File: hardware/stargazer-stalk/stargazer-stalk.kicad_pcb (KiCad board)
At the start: 2 copper layers, 8 parts, among them U10 pmod-interface-type-2a, U12 pmod-interface-type-2a, U14 pmod-interface-type-2a, U18 pmod-interface-type-2a, U2 pmod-interface-type-2a, U4 pmod-interface-type-2a, U6 pmod-interface-type-2a, U8 pmod-interface-type-2a

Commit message: Working before reworking to a 4 card system
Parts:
- added C1: 0.1uF, Capacitor_SMD:C_0805_2012Metric, F.Cu at (204.5, 20.3)
- added C10: 0.1uF, Capacitor_SMD:C_0805_2012Metric, F.Cu at (115.7, 131.3)
- added C2: 0.1uF, Capacitor_SMD:C_0805_2012Metric, F.Cu at (125.7, 60.3)
- added C3: 0.1uF, Capacitor_SMD:C_0805_2012Metric, F.Cu at (154.1, 126.1)
- added C4: 0.1uF, Capacitor_SMD:C_0805_2012Metric, F.Cu at (87.6, 60.9)
- added C5: 0.1uF, Capacitor_SMD:C_0805_2012Metric, F.Cu at (189.6, 100.5)
- added C6: 0.1uF, Capacitor_SMD:C_0805_2012Metric, F.Cu at (49.9, 90.6)
- added C7: 0.1uF, Capacitor_SMD:C_0805_2012Metric, F.Cu at (159.7, 63.9)
- added C8: 0.1uF, Capacitor_SMD:C_0805_2012Metric, F.Cu at (87.0, 131.9)
- added J1: swd-basic, Connector_PinHeader_2.54mm:PinHeader_1x04_P2.54mm_Vertical, F.Cu at (125.0, 126.7)
- added J2: swd-basic, Connector_PinHeader_2.54mm:PinHeader_1x04_P2.54mm_Vertical, F.Cu at (116.8, 51.0)
- added J3: swd-basic, Connector_PinHeader_2.54mm:PinHeader_1x04_P2.54mm_Vertical, F.Cu at (165.5, 126.2)
- added J4: swd-basic, Connector_PinHeader_2.54mm:PinHeader_1x04_P2.54mm_Vertical, F.Cu at (78.7, 51.5)
- added J5: swd-basic, Connector_PinHeader_2.54mm:PinHeader_1x04_P2.54mm_Vertical, F.Cu at (189.7, 89.1)
- added J6: swd-basic, Connector_PinHeader_2.54mm:PinHeader_1x04_P2.54mm_Vertical, F.Cu at (49.8, 102.0)
- added J7: swd-basic, Connector_PinHeader_2.54mm:PinHeader_1x04_P2.54mm_Vertical, F.Cu at (155.4, 51.5)
- added J8: swd-basic, Connector_PinHeader_2.54mm:PinHeader_1x04_P2.54mm_Vertical, F.Cu at (74.7, 132.2)
- added JP1: SolderJumper_3_Bridged12, Jumper:SolderJumper-3_P1.3mm_Bridged12_RoundedPad1.0x1.5mm, F.Cu at (182.7, 32.3)
- added JP10: SolderJumper_2_Bridged, Jumper:SolderJumper-2_P1.3mm_Bridged_RoundedPad1.0x1.5mm, F.Cu at (197.7, 32.4)
- added JP11: SolderJumper_2_Bridged, Jumper:SolderJumper-2_P1.3mm_Bridged_RoundedPad1.0x1.5mm, F.Cu at (203.4, 26.5)
- added JP2: SolderJumper_3_Bridged12, Jumper:SolderJumper-3_P1.3mm_Bridged12_RoundedPad1.0x1.5mm, F.Cu at (195.0, 20.6)
- added JP3: SolderJumper_3_Bridged12, Jumper:SolderJumper-3_P1.3mm_Bridged12_RoundedPad1.0x1.5mm, F.Cu at (188.3, 32.3)
- added JP4: SolderJumper_2_Bridged, Jumper:SolderJumper-2_P1.3mm_Bridged_RoundedPad1.0x1.5mm, F.Cu at (208.8, 24.2)
- added JP5: SolderJumper_2_Bridged, Jumper:SolderJumper-2_P1.3mm_Bridged_RoundedPad1.0x1.5mm, F.Cu at (202.1, 33.6)
- added JP6: SolderJumper_2_Bridged, Jumper:SolderJumper-2_P1.3mm_Bridged_RoundedPad1.0x1.5mm, F.Cu at (207.8, 27.7)
- added JP7: SolderJumper_2_Bridged, Jumper:SolderJumper-2_P1.3mm_Bridged_RoundedPad1.0x1.5mm, F.Cu at (207.6, 31.3)
- added JP8: SolderJumper_2_Bridged, Jumper:SolderJumper-2_P1.3mm_Bridged_RoundedPad1.0x1.5mm, F.Cu at (208.8, 20.6)
- added JP9: SolderJumper_2_Bridged, Jumper:SolderJumper-2_P1.3mm_Bridged_RoundedPad1.0x1.5mm, F.Cu at (203.2, 30.1)
- added R1: 100k, Resistor_SMD:R_0805_2012Metric, F.Cu at (121.1, 63.3)
- added R10: 10k, Resistor_SMD:R_0805_2012Metric, F.Cu at (204.5, 23.3)
- added R11: 10k, Resistor_SMD:R_0805_2012Metric, F.Cu at (193.4, 34.9)
- added R12: 10k, Resistor_SMD:R_0805_2012Metric, F.Cu at (198.8, 29.2)
- added R13: 100k, Resistor_SMD:R_0805_2012Metric, F.Cu at (83.0, 63.9)
- added R14: 100k, Resistor_SMD:R_0805_2012Metric, F.Cu at (198.7, 98.4)
- added R15: 100k, Resistor_SMD:R_0805_2012Metric, F.Cu at (194.0, 101.4)
- added R16: 100k, Resistor_SMD:R_0805_2012Metric, F.Cu at (194.2, 98.4)
- added R17: 100k, Resistor_SMD:R_0805_2012Metric, F.Cu at (40.8, 92.7)
- added R18: 100k, Resistor_SMD:R_0805_2012Metric, F.Cu at (45.5, 89.7)
- added R19: 100k, Resistor_SMD:R_0805_2012Metric, F.Cu at (45.2, 92.7)
- added R2: 100k, Resistor_SMD:R_0805_2012Metric, F.Cu at (121.3, 60.3)
- added R20: 100k, Resistor_SMD:R_0805_2012Metric, F.Cu at (164.4, 60.9)
- added R21: 10k, Resistor_SMD:R_0805_2012Metric, F.Cu at (193.4, 32.0)
- added R22: 10k, Resistor_SMD:R_0805_2012Metric, F.Cu at (194.4, 28.8)
- added R23: 10k, Resistor_SMD:R_0805_2012Metric, F.Cu at (200.1, 23.3)
- added R24: 10k, Resistor_SMD:R_0805_2012Metric, F.Cu at (200.1, 20.3)
- added R25: 100k, Resistor_SMD:R_0805_2012Metric, F.Cu at (159.9, 60.9)
- added R26: 100k, Resistor_SMD:R_0805_2012Metric, F.Cu at (155.3, 62.9)
- added R27: 100k, Resistor_SMD:R_0805_2012Metric, F.Cu at (84.1, 127.2)
- added R28: 100k, Resistor_SMD:R_0805_2012Metric, F.Cu at (87.0, 127.5)
- added R29: 100k, Resistor_SMD:R_0805_2012Metric, F.Cu at (85.0, 122.8)
- added R3: 100k, Resistor_SMD:R_0805_2012Metric, F.Cu at (116.7, 62.4)
- added R33: 100k, Resistor_SMD:R_0805_2012Metric, F.Cu at (112.7, 131.0)
- added R34: 100k, Resistor_SMD:R_0805_2012Metric, F.Cu at (115.7, 135.7)
- added R35: 100k, Resistor_SMD:R_0805_2012Metric, F.Cu at (113.6, 126.6)
- added R4: 100k, Resistor_SMD:R_0805_2012Metric, F.Cu at (156.2, 135.2)
- added R5: 100k, Resistor_SMD:R_0805_2012Metric, F.Cu at (153.2, 130.5)
- added R6: 100k, Resistor_SMD:R_0805_2012Metric, F.Cu at (156.2, 130.8)
- added R7: 100k, Resistor_SMD:R_0805_2012Metric, F.Cu at (78.6, 62.9)
- added R8: 100k, Resistor_SMD:R_0805_2012Metric, F.Cu at (83.2, 60.9)
- added R9: 10k, Resistor_SMD:R_0805_2012Metric, F.Cu at (199.1, 26.2)
- added TP1: TestPoint, Connector_PinHeader_2.54mm:PinHeader_1x01_P2.54mm_Vertical, F.Cu at (194.5, 25.0)
- added U1: SN74LVC125AD, Package_SO:SOIC-14_3.9x8.7mm_P1.27mm, F.Cu at (108.0, 80.0)
- added U11: SN74LVC125AD, Package_SO:SOIC-14_3.9x8.7mm_P1.27mm, F.Cu at (146.1, 80.0)
- added U13: SN74LVC125AD, Package_SO:SOIC-14_3.9x8.7mm_P1.27mm, F.Cu at (95.2, 110.5)
- added U16: PCF8574, stargazer-stalk:SOIC127P1032X265-16N, F.Cu at (186.0, 24.7)
- added U17: SN74LVC125AD, Package_SO:SOIC-14_3.9x8.7mm_P1.27mm, F.Cu at (133.3, 110.5)
- added U3: SN74LVC125AD, Package_SO:SOIC-14_3.9x8.7mm_P1.27mm, F.Cu at (171.4, 110.5)
- added U5: SN74LVC125AD, Package_SO:SOIC-14_3.9x8.7mm_P1.27mm, F.Cu at (69.8, 80.0)
- added U7: SN74LVC125AD, Package_SO:SOIC-14_3.9x8.7mm_P1.27mm, F.Cu at (174.0, 82.5)
- added U9: SN74LVC125AD, Package_SO:SOIC-14_3.9x8.7mm_P1.27mm, F.Cu at (67.3, 108.0)
- moved U10 89.3 mm to (69.8, 102.9), turned to 180 degrees
- moved U6 83.9 mm to (74.9, 82.5)
- moved U18 63.5 mm to (128.3, 108.0), turned to 270 degrees
- moved U4 54.3 mm to (166.4, 108.0), turned to 270 degrees
- moved U12 42.2 mm to (151.1, 82.5), turned to 90 degrees
- moved U2 30.7 mm to (113.0, 82.5)
- moved U14 8.52 mm to (90.2, 108.0)
- moved U8 8.52 mm to (171.4, 87.6)
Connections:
- U10 pad 1: /card-6/CSn1 -> /card-6/CSn
- U10 pad 10: /card-6/SWCLK1 -> /card-6/SWCLK
- U10 pad 2: /card-6/COPI1 -> /card-6/COPI
- U10 pad 3: /card-6/CIPO1 -> /card-6/CIPO
- U10 pad 4: /card-6/SCK1 -> /card-6/SCK
- U10 pad 7: /card-6/GO1 -> /card-6/GO
- U10 pad 8: /card-6/RST1 -> /card-6/RST
- U10 pad 9: /card-6/SWDIO1 -> /card-6/SWDIO
- U12 pad 1: /card-7/CSn1 -> /card-7/CSn
- U12 pad 10: /card-7/SWCLK1 -> /card-7/SWCLK
- U12 pad 2: /card-7/COPI1 -> /card-7/COPI
- U12 pad 3: /card-7/CIPO1 -> /card-7/CIPO
- U12 pad 4: /card-7/SCK1 -> /card-7/SCK
- U12 pad 7: /card-7/GO1 -> /card-7/GO
- U12 pad 8: /card-7/RST1 -> /card-7/RST
- U12 pad 9: /card-7/SWDIO1 -> /card-7/SWDIO
- U14 pad 1: /card-8/CSn1 -> /card-8/CSn
- U14 pad 10: /card-8/SWCLK1 -> /card-8/SWCLK
- U14 pad 2: /card-8/COPI1 -> /card-8/COPI
- U14 pad 3: /card-8/CIPO1 -> /card-8/CIPO
- U14 pad 4: /card-8/SCK1 -> /card-8/SCK
- U14 pad 7: /card-8/GO1 -> /card-8/GO
- U14 pad 8: /card-8/RST1 -> /card-8/RST
- U14 pad 9: /card-8/SWDIO1 -> /card-8/SWDIO
- U18 pad 1: /card-1/CSn1 -> /card-1/CSn
- U18 pad 10: /card-1/SWCLK1 -> /card-1/SWCLK
- U18 pad 2: /card-1/COPI1 -> /card-1/COPI
- U18 pad 3: /card-1/CIPO1 -> /card-1/CIPO
- U18 pad 4: /card-1/SCK1 -> /card-1/SCK
- U18 pad 7: /card-1/GO1 -> /card-1/GO
- U18 pad 8: /card-1/RST1 -> /card-1/RST
- U18 pad 9: /card-1/SWDIO1 -> /card-1/SWDIO
- U2 pad 1: /card-2/CSn1 -> /card-2/CSn
- U2 pad 10: /card-2/SWCLK1 -> /card-2/SWCLK
- U2 pad 2: /card-2/COPI1 -> /card-2/COPI
- U2 pad 3: /card-2/CIPO1 -> /card-2/CIPO
- U2 pad 4: /card-2/SCK1 -> /card-2/SCK
- U2 pad 7: /card-2/GO1 -> /card-2/GO
- U2 pad 8: /card-2/RST1 -> /card-2/RST
- U2 pad 9: /card-2/SWDIO1 -> /card-2/SWDIO
- U4 pad 1: /card-3/CSn1 -> /card-3/CSn
- U4 pad 10: /card-3/SWCLK1 -> /card-3/SWCLK
- U4 pad 2: /card-3/COPI1 -> /card-3/COPI
- U4 pad 3: /card-3/CIPO1 -> /card-3/CIPO
- U4 pad 4: /card-3/SCK1 -> /card-3/SCK
- U4 pad 7: /card-3/GO1 -> /card-3/GO
- U4 pad 8: /card-3/RST1 -> /card-3/RST
- U4 pad 9: /card-3/SWDIO1 -> /card-3/SWDIO
- U6 pad 1: /card-4/CSn1 -> /card-4/CSn
- U6 pad 10: /card-4/SWCLK1 -> /card-4/SWCLK
- U6 pad 2: /card-4/COPI1 -> /card-4/COPI
- U6 pad 3: /card-4/CIPO1 -> /card-4/CIPO
- U6 pad 4: /card-4/SCK1 -> /card-4/SCK
- U6 pad 7: /card-4/GO1 -> /card-4/GO
- U6 pad 8: /card-4/RST1 -> /card-4/RST
- U6 pad 9: /card-4/SWDIO1 -> /card-4/SWDIO
- U8 pad 1: /card-5/CSn1 -> /card-5/CSn
- U8 pad 10: /card-5/SWCLK1 -> /card-5/SWCLK
- U8 pad 2: /card-5/COPI1 -> /card-5/COPI
- U8 pad 3: /card-5/CIPO1 -> /card-5/CIPO
- U8 pad 4: /card-5/SCK1 -> /card-5/SCK
- U8 pad 7: /card-5/GO1 -> /card-5/GO
- U8 pad 8: /card-5/RST1 -> /card-5/RST
- U8 pad 9: /card-5/SWDIO1 -> /card-5/SWDIO
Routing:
- net +5V: track 0.00 -> 264.2 mm, vias 0 -> 12
- net +3V3: track 0.00 -> 219.0 mm
- net GND: track 0.00 -> 1.30 mm, vias 0 -> 1
- added copper zone on B.Cu, net GND
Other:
- board outline added: 114.3 x 38.1 mm

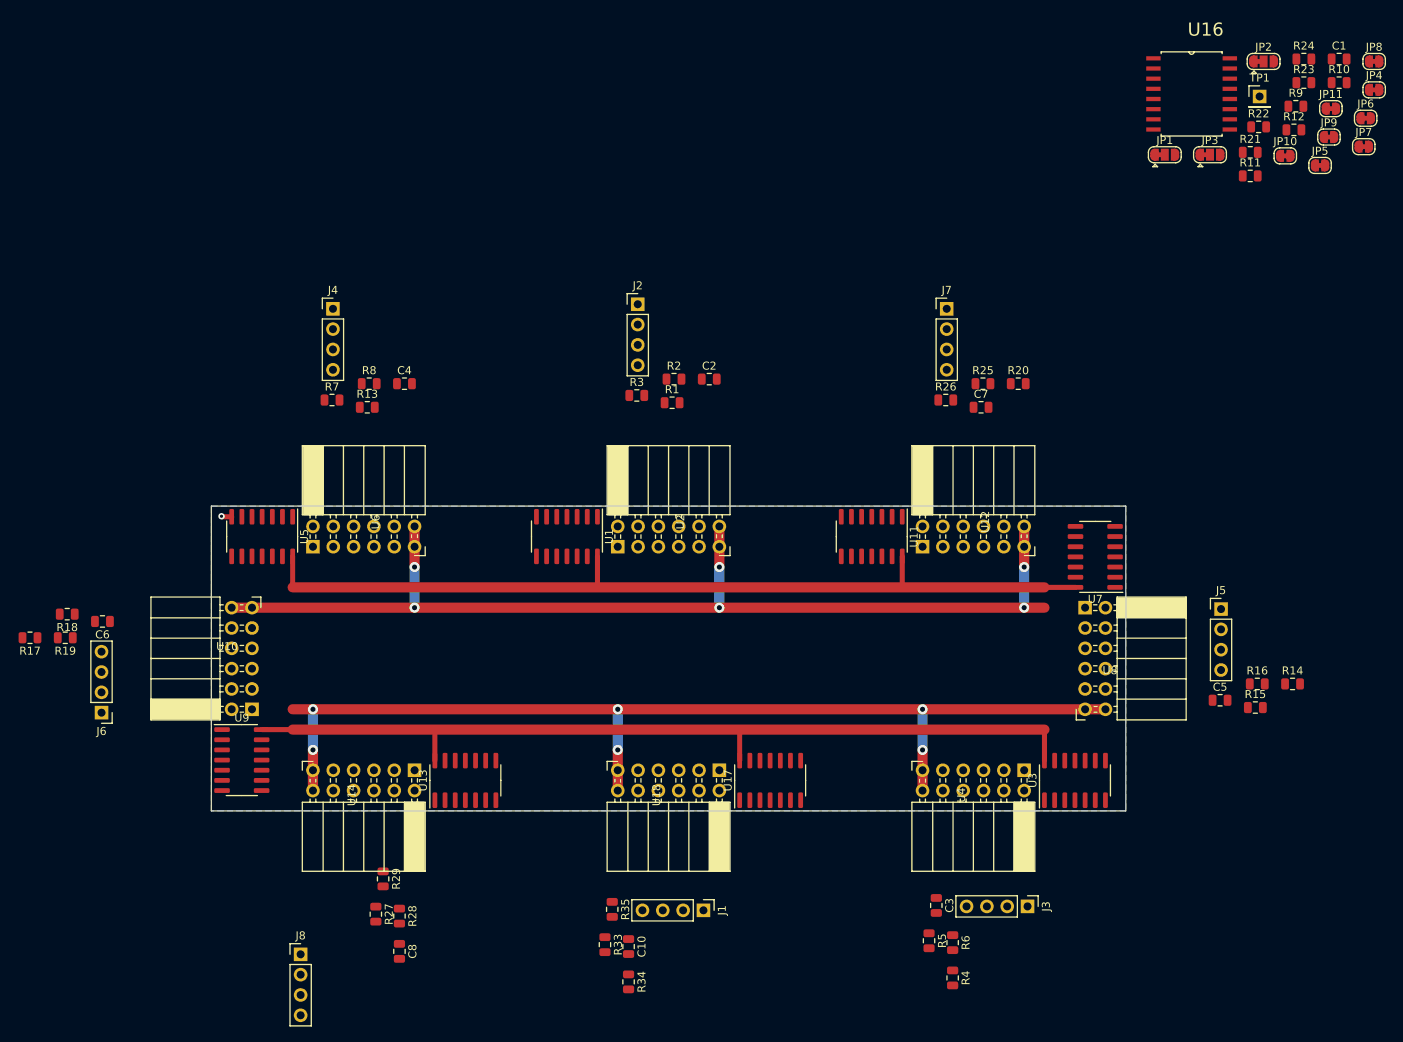
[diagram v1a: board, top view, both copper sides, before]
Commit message: Finished routing, but it's probably too much for 2 layers
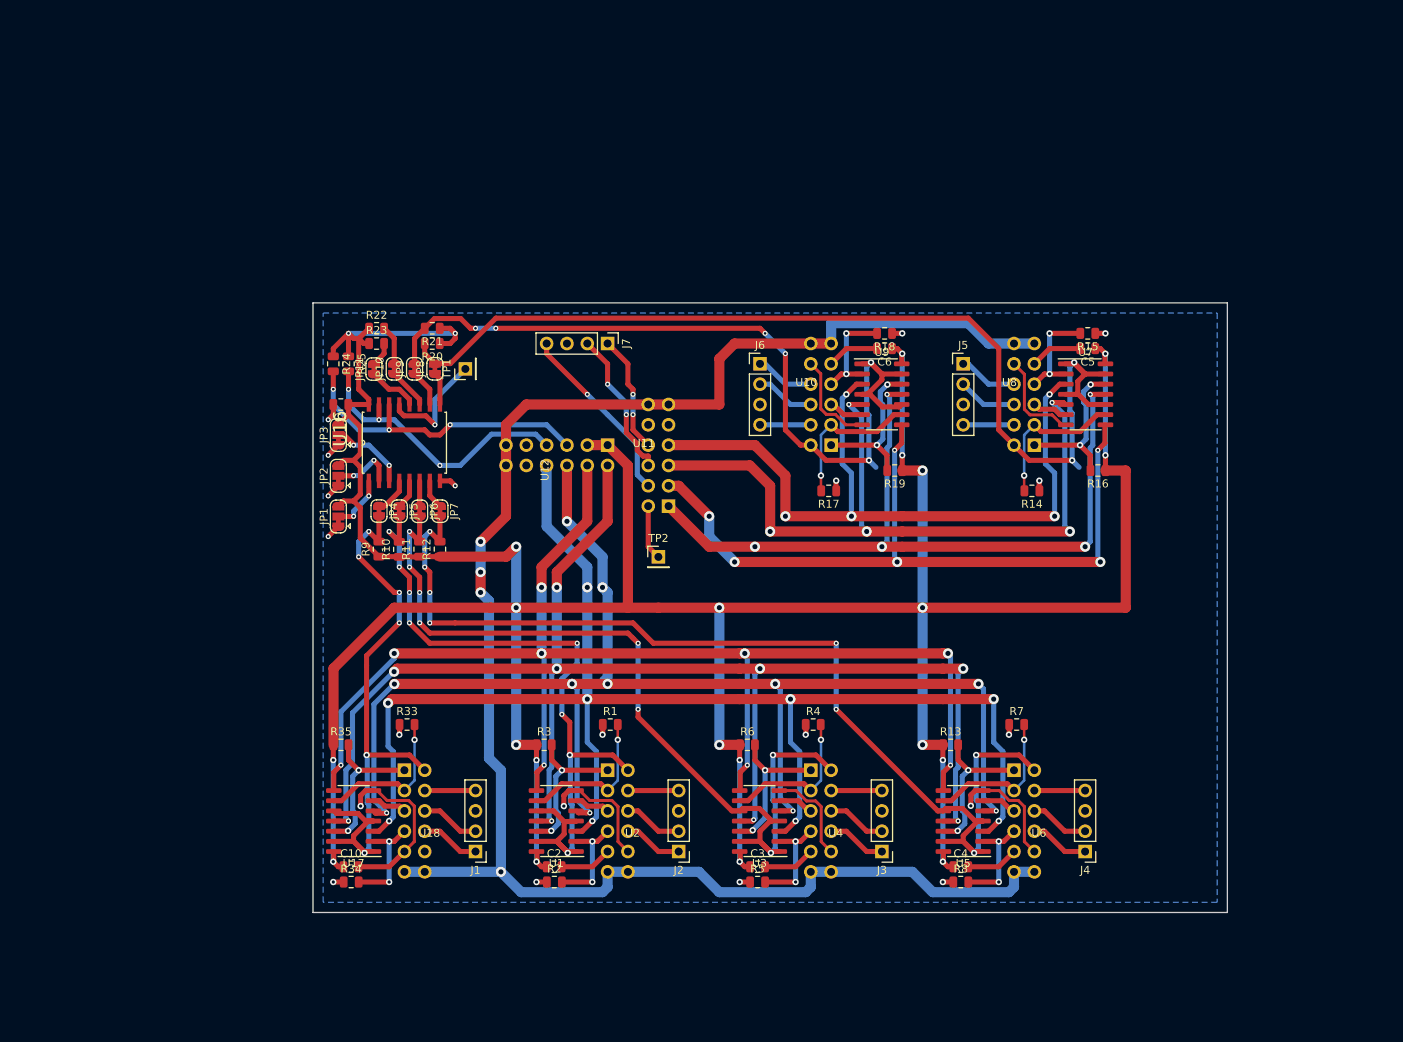
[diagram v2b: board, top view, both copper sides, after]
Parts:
- removed C7, C8: 0.1uF, Capacitor_SMD:C_0805_2012Metric
- removed J8: swd-basic, Connector_PinHeader_2.54mm:PinHeader_1x04_P2.54mm_Vertical
- removed R26, R27, R28, R29: 100k, Resistor_SMD:R_0805_2012Metric
- removed U13: SN74LVC125AD, Package_SO:SOIC-14_3.9x8.7mm_P1.27mm
- removed U14: pmod-interface-type-2a, stargazer-stalk:pmod-double
- added TP2: TestPoint, Connector_PinHeader_2.54mm:PinHeader_1x01_P2.54mm_Vertical, F.Cu at (119.4, 82.5)
- R20: value 100k -> 10k
- R24: value 10k -> R
- R25: value 100k -> R
- U10, U18, U2, U4, U6, U8: footprint stargazer-stalk:pmod-double -> stargazer-stalk:pmod-double-vertical
- U11: value SN74LVC125AD -> pmod-interface-type-2a-arb; footprint Package_SO:SOIC-14_3.9x8.7mm_P1.27mm -> stargazer-stalk:pmod-double-vertical
- U12: value pmod-interface-type-2a -> pmod-interface-type-6a-arb; footprint stargazer-stalk:pmod-double -> stargazer-stalk:pmod-double-vertical
- moved JP4 135.1 mm to (84.5, 76.8), turned to 270 degrees
- moved C1 132.1 mm to (79.7, 63.5), turned to 180 degrees
- moved R10 131.2 mm to (87.0, 81.6), turned to 90 degrees
- moved JP6 128.1 mm to (89.5, 76.8), turned to 270 degrees
- moved R9 127.3 mm to (84.5, 81.6), turned to 90 degrees
- moved R24 127.2 mm to (78.7, 58.4), turned to 270 degrees
- moved JP2 126.7 mm to (79.4, 72.4), turned to 90 degrees
- moved JP7 124.1 mm to (92.1, 76.8), turned to 270 degrees
- moved JP11 124.0 mm to (83.8, 59.1), turned to 90 degrees
- moved JP8 123.5 mm to (91.4, 59.0), turned to 90 degrees
- moved JP5 122.9 mm to (87.0, 76.8), turned to 270 degrees
- moved R23 120.4 mm to (84.2, 55.9)
- moved R12 118.9 mm to (92.1, 81.6), turned to 90 degrees
- moved JP9 117.9 mm to (88.9, 59.0), turned to 90 degrees
- moved J4 115.9 mm to (172.7, 119.4), turned to 180 degrees
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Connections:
- J7 pad 1: /card-7/SWCLK -> /SWCLK-ARB
- J7 pad 2: /card-7/SWDIO -> /SWDIO-ARB
- J7 pad 4: /card-7/RST -> /RST-ARB
- R10 pad 2: Net-(JP5-Pad1) -> /GO2
- R11 pad 2: Net-(JP6-Pad1) -> /GO3
- R12 pad 2: Net-(JP7-Pad1) -> /GO4
- R20 pad 1: GND -> +3V3
- R20 pad 2: /card-7/COPI -> /GO5
- R21 pad 2: Net-(JP8-Pad1) -> /GO6
- R22 pad 2: Net-(JP9-Pad1) -> /GO7
- R23 pad 2: Net-(JP10-Pad1) -> /GO8
- R24 pad 2: Net-(JP11-Pad1) -> /PORT-SCL
- R25 pad 1: GND -> +3V3
- R25 pad 2: /card-7/SCK -> /PORT-SDA
- R9 pad 2: Net-(JP4-Pad1) -> /GO1
- U1 pad 1: /card-2/GO -> /GO2
- U1 pad 10: /card-2/GO -> /GO2
- U1 pad 11: /CSnx -> /OPT-CSnx
- U1 pad 13: /card-2/GO -> /GO2
- U1 pad 3: /SCKx -> /OPT-SCKx
- U1 pad 4: /card-2/GO -> /GO2
- U1 pad 5: /CIPOx -> /OPT-CIPOx
- U1 pad 8: /COPIx -> /OPT-COPIx
- U10 pad 7: /card-6/GO -> /GO6
- U11 pad 1: /card-7/GO -> /CSnx
- U11 pad 10: /card-7/GO -> /SWCLK-ARB
- U11 pad 11: /CSnx -> GND
- U11 pad 12: /card-7/CSn -> +5V
- U11 pad 2: /card-7/SCK -> /COPIx
- U11 pad 3: /SCKx -> /CIPOx
- U11 pad 4: /card-7/GO -> /SCKx
- U11 pad 5: /CIPOx -> GND
- U11 pad 6: /card-7/CIPO -> +5V
- U11 pad 7: GND -> /MISC-ARB
- U11 pad 8: /COPIx -> /RST-ARB
- U11 pad 9: /card-7/COPI -> /SWDIO-ARB
- U12 pad 1: /card-7/CSn -> +3V3
- U12 pad 10: /card-7/SWCLK -> /OPT-SCKx
- U12 pad 2: /card-7/COPI -> +3V3
- U12 pad 3: /card-7/CIPO -> /PORT-SCL
- U12 pad 4: /card-7/SCK -> /PORT-SDA
- U12 pad 7: /card-7/GO -> /OPT-CSnx
- U12 pad 8: /card-7/RST -> /OPT-COPIx
- U12 pad 9: /card-7/SWDIO -> /OPT-CIPOx
- U17 pad 1: /card-1/GO -> /GO1
- U17 pad 10: /card-1/GO -> /GO1
- U17 pad 11: /CSnx -> /OPT-CSnx
- U17 pad 13: /card-1/GO -> /GO1
- U17 pad 3: /SCKx -> /OPT-SCKx
- U17 pad 4: /card-1/GO -> /GO1
- U17 pad 5: /CIPOx -> /OPT-CIPOx
- U17 pad 8: /COPIx -> /OPT-COPIx
- U18 pad 7: /card-1/GO -> /GO1
- U2 pad 7: /card-2/GO -> /GO2
- U3 pad 1: /card-3/GO -> /GO3
- U3 pad 10: /card-3/GO -> /GO3
- U3 pad 11: /CSnx -> /OPT-CSnx
- U3 pad 13: /card-3/GO -> /GO3
- U3 pad 3: /SCKx -> /OPT-SCKx
- U3 pad 4: /card-3/GO -> /GO3
- U3 pad 5: /CIPOx -> /OPT-CIPOx
- U3 pad 8: /COPIx -> /OPT-COPIx
- U4 pad 7: /card-3/GO -> /GO3
- U5 pad 1: /card-4/GO -> /GO4
- U5 pad 10: /card-4/GO -> /GO4
- U5 pad 11: /CSnx -> /OPT-CSnx
- U5 pad 13: /card-4/GO -> /GO4
- U5 pad 3: /SCKx -> /OPT-SCKx
- U5 pad 4: /card-4/GO -> /GO4
- U5 pad 5: /CIPOx -> /OPT-CIPOx
- U5 pad 8: /COPIx -> /OPT-COPIx
- U6 pad 7: /card-4/GO -> /GO4
- U7 pad 1: /card-5/GO -> /GO5
- U7 pad 10: /card-5/GO -> /GO5
- U7 pad 13: /card-5/GO -> /GO5
- U7 pad 4: /card-5/GO -> /GO5
- U8 pad 7: /card-5/GO -> /GO5
- U9 pad 1: /card-6/GO -> /GO6
- U9 pad 10: /card-6/GO -> /GO6
- U9 pad 13: /card-6/GO -> /GO6
- U9 pad 4: /card-6/GO -> /GO6
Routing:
- net +3V3: track 219.0 -> 433.5 mm, vias 0 -> 22
- net /OPT-CSnx: track 0.00 -> 186.3 mm, vias 0 -> 9
- net /OPT-SCKx: track 0.00 -> 180.2 mm, vias 0 -> 9
- net /OPT-CIPOx: track 0.00 -> 178.3 mm, vias 0 -> 11
- net /OPT-COPIx: track 0.00 -> 168.3 mm, vias 0 -> 9
- net GND: track 1.30 -> 146.7 mm, vias 1 -> 20
- net /GO4: track 0.00 -> 133.5 mm, vias 0 -> 8
- net /GO5: track 0.00 -> 128.0 mm, vias 0 -> 2
- net /GO3: track 0.00 -> 108.2 mm, vias 0 -> 8
- net /GO6: track 0.00 -> 104.9 mm, vias 0 -> 6
- net /CSnx: track 0.00 -> 97.0 mm, vias 0 -> 5
- net /COPIx: track 0.00 -> 94.7 mm, vias 0 -> 6
- net /CIPOx: track 0.00 -> 94.2 mm, vias 0 -> 5
- net /SCKx: track 0.00 -> 91.8 mm, vias 0 -> 5
- net /GO2: track 0.00 -> 91.1 mm, vias 0 -> 8
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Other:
- board size 114.3 x 38.1 mm -> 114.3 x 76.2 mm
